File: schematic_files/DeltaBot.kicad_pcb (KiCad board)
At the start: 2 copper layers, 241.5 x 110.5 mm, 15 parts, among them J1 USB C PD Modulle, J2 LIDAR, J3 MOTOR_L, J4 MOTOR_R, SW1 SW_SPDT, U1 RPLIDAR C1, U1 Radxa_ROCK5B, U2 Buck Converter

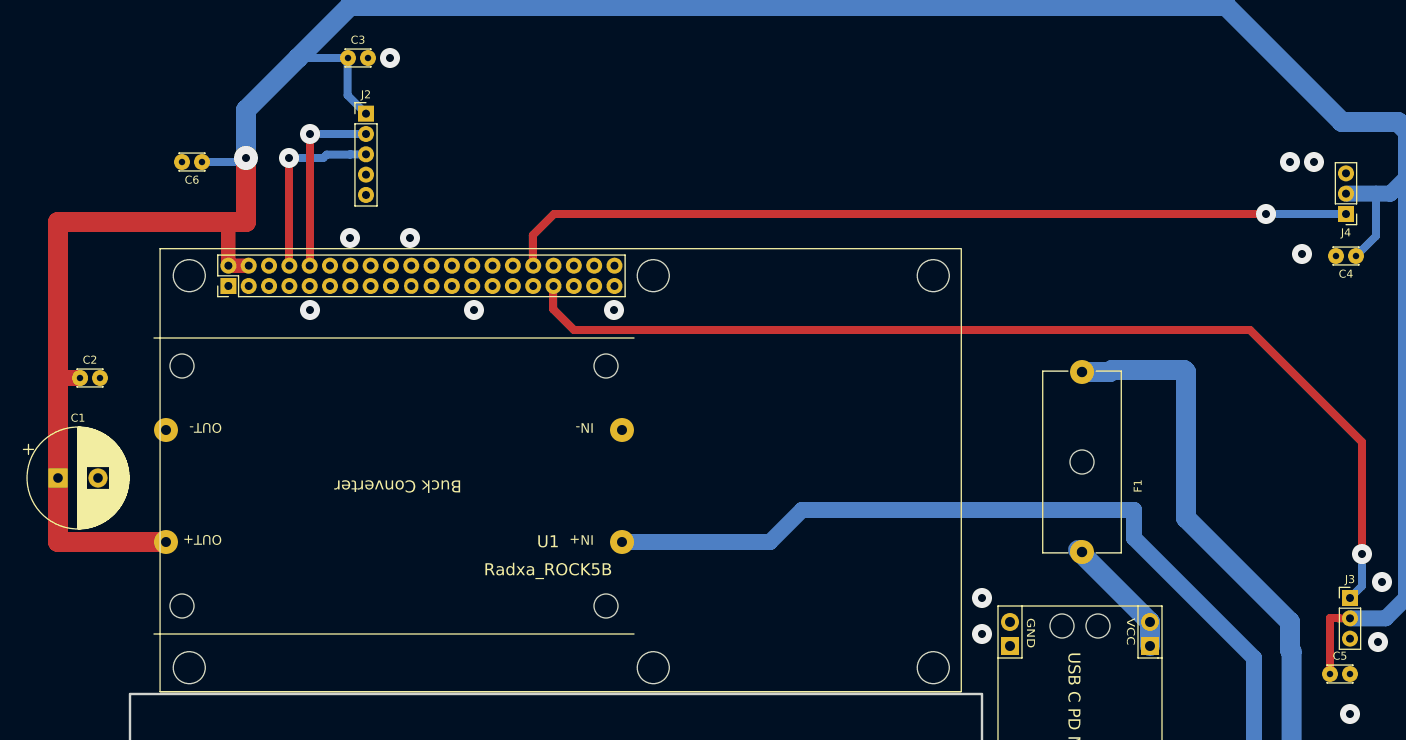
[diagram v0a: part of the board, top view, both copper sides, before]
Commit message: Updated the PCB so that all pads can be soldered without plating through.
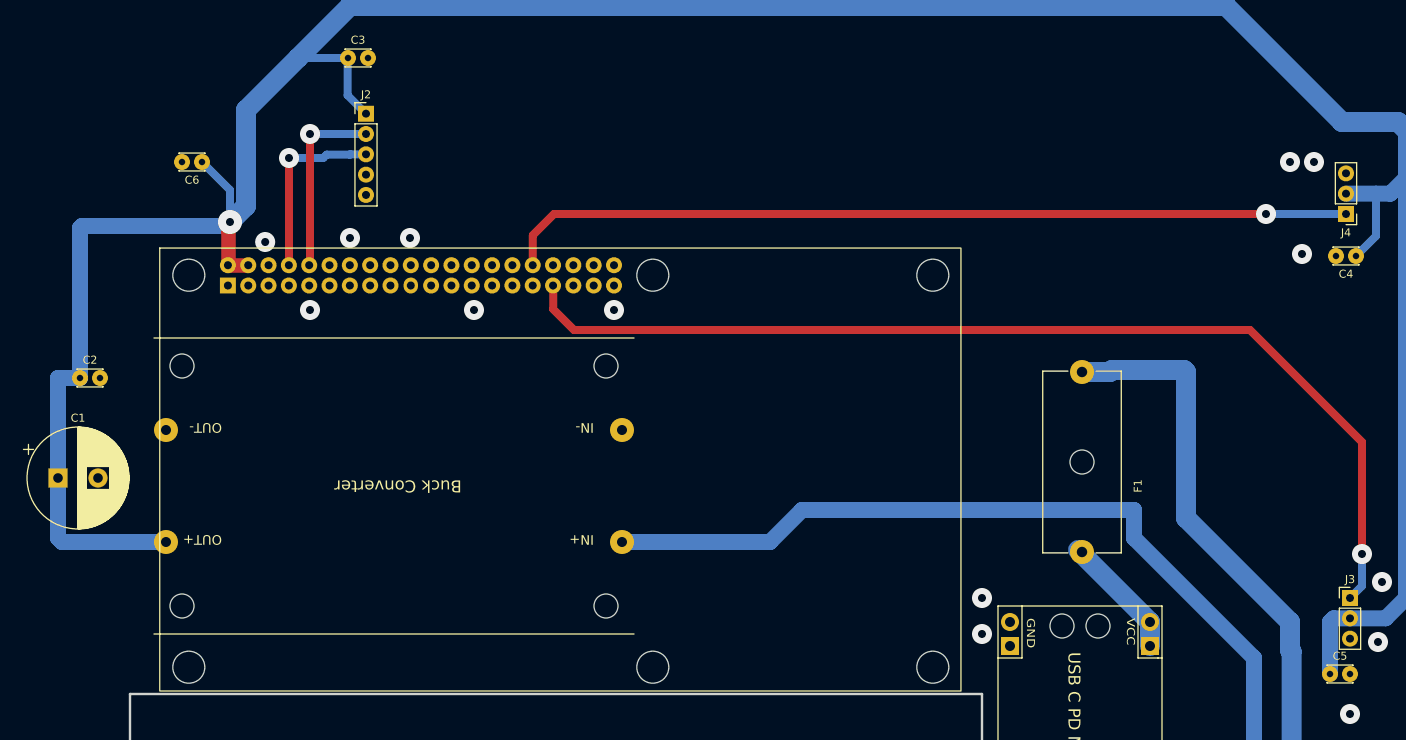
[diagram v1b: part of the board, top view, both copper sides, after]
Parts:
- U1: footprint deltabot:ROCK_5B -> DeltaBotFootprints:ROCK_5B; moved to B.Cu
- moved U1 3.09 mm to (104.8, 108.9), turned to 180 degrees
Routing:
- net +5V: track 372.2 -> 370.4 mm

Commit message: Added an LED to it.
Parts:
- added D1: LED, LED_THT:LED_D5.0mm_Clear, F.Cu at (194.2, 91.0)
- added R1: 330R, Resistor_THT:R_Axial_DIN0207_L6.3mm_D2.5mm_P10.16mm_Horizontal, F.Cu at (202.8, 75.9)
- J2: value LIDAR -> Conn_01x05; footprint deltabot:PinHeader_1x05_P2.54mm_Vertical -> DeltaBotFootprints:PinHeader_1x05_P2.54mm_Vertical
- moved F1 0.25 mm to (168.5, 86.0)
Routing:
- net Net-(D1-A): track 0.00 -> 8.02 mm
- net +5V: track 370.4 -> 374.6 mm
- net PWM_L: track 130.8 -> 129.1 mm

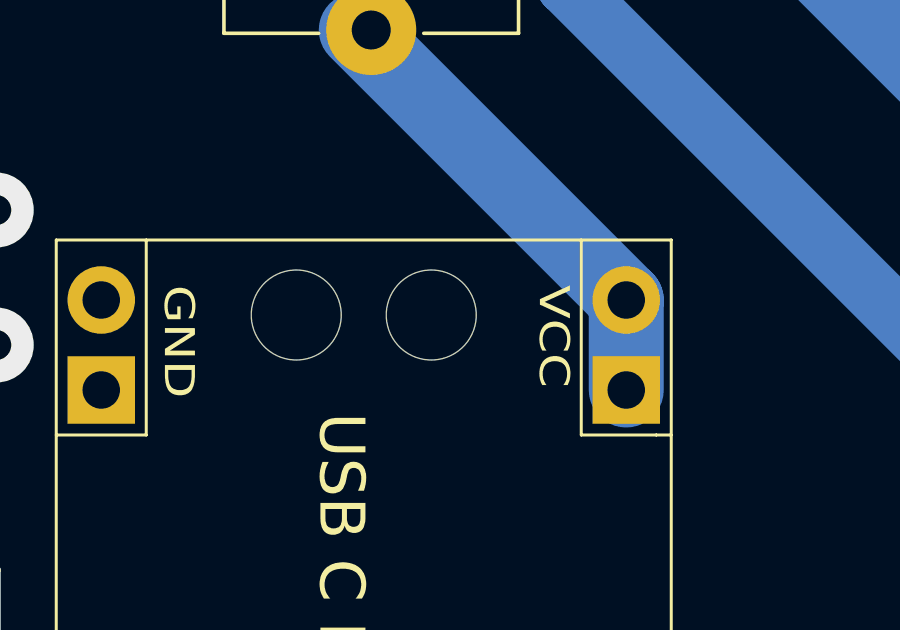
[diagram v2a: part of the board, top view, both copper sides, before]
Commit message: Fixed the USB PD module footprint.
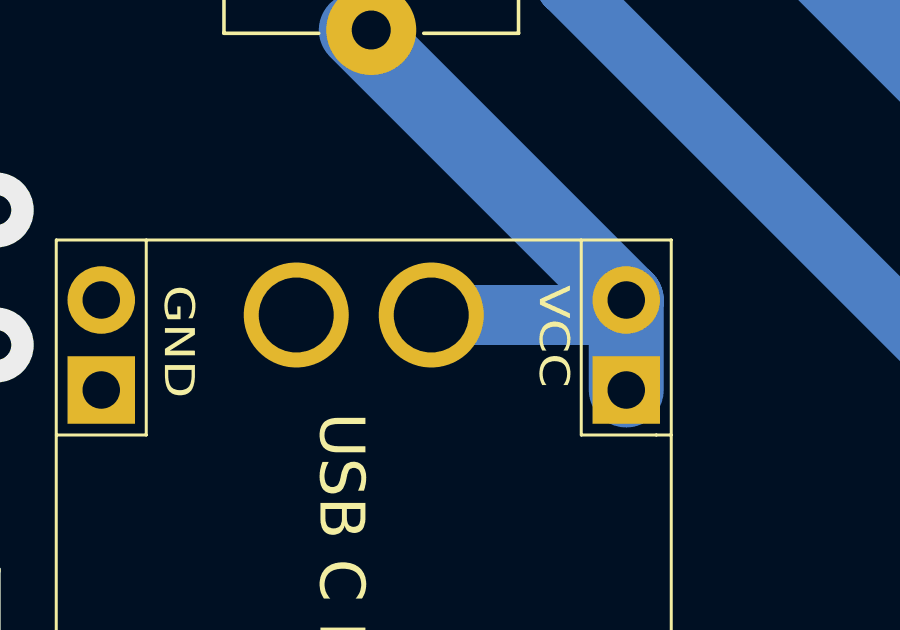
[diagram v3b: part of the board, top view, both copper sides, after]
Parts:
- J1: footprint deltabot:USB_C -> DeltaBotFootprints:USB_C
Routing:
- net Net-(J1-VCC): track 15.7 -> 22.4 mm
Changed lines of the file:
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@@
 		)
 	)
-	(footprint "deltabot:USB_C"
+	(footprint "DeltaBotFootprints:USB_C"
 		(layer "F.Cu")
 		(at 168.5 130.5 -90)
@@
 			(unit
 				(name "A")
-				(pins "1" "2")
+				(pins "3" "4" "1" "2")
 			)
 		)
@@
 			)
 		)
-		(pad "" np_thru_hole circle
-			(at -12.5 -2 270)
-			(size 3 3)
-			(drill 3)
-			(layers "*.Cu" "*.Mask")
-		)
-		(pad "" np_thru_hole circle
-			(at -12.5 2.5 270)
-			(size 2.5 2.5)
-			(drill 3)
-			(layers "*.Cu" "*.Mask")
-		)
 		(pad "1" thru_hole circle
 			(at -13 -8.5 270)
@@
 			(net "Net-(J1-VCC)")
 			(pinfunction "VCC_1")
-			(pintype "passive")
+			(pintype "power_out")
 			(thermal_bridge_angle 90)
 		)
@@
 			(net "Net-(J1-VCC)")
 			(pinfunction "VCC_1")
-			(pintype "passive")
+			(pintype "power_out")
 		)
 		(pad "2" thru_hole circle
@@
 			(net "GND")
 			(pinfunction "GND_2")
-			(pintype "passive")
+			(pintype "power_out")
 			(thermal_bridge_angle 90)
 		)
@@
 			(net "GND")
 			(pinfunction "GND_2")
-			(pintype "passive")
+			(pintype "power_out")
+		)
+		(pad "3" thru_hole circle
+			(at -12.5 -2 270)
+			(size 3.5 3.5)
+			(drill 2.5)
+			(layers "*.Cu" "*.Mask")
+			(remove_unused_layers no)
+			(net "Net-(J1-VCC)")
+			(pinfunction "VCC_3")
+			(pintype "power_out")
+		)
+		(pad "4" thru_hole circle
+			(at -12.5 2.5 270)
+			(size 3.5 3.5)
+			(drill 2.5)
+			(layers "*.Cu" "*.Mask")
+			(remove_unused_layers no)
+			(net "GND")
+			(pinfunction "GND_4")
+			(pintype "power_out")
 		)
 		(embedded_fonts no)
@@
 		(layer "B.Cu")
 		(net "Net-(J1-VCC)")
+	)
+	(segment
+		(start 176.5 118)
+		(end 177 117.5)
+		(width 2)
+		(layer "B.Cu")
+		(net "Net-(J1-VCC)")
+	)
+	(segment
+		(start 170.5 118)
+		(end 176.5 118)
+		(width 2)
+		(layer "B.Cu")
+		(net "Net-(J1-VCC)")

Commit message: Updated the DollaTek Buck converter.
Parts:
- U2: footprint deltabot:BUCK_CONV -> DeltaBotFootprints:BUCK_CONV
- moved U2 7.50 mm to (90.5, 100.5)
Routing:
- net +9V: track 106.4 -> 99.9 mm
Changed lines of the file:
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@@
 		)
 	)
-	(footprint "deltabot:BUCK_CONV"
+	(footprint "DeltaBotFootprints:BUCK_CONV"
 		(layer "F.Cu")
-		(at 83 100.5 180)
+		(at 90.5 100.5 180)
 		(property "Reference" "U2"
 			(at 0 -3.5 180)
@@
 			)
 		)
-		(sheetname "/")
-		(sheetfile "DeltaBot.kicad_sch")
-		(units
-			(unit
-				(name "A")
-				(pins "1" "2" "3" "4")
+		(property "Field4" "${REFERENCE}"
+			(at 0 -7.5 180)
+			(unlocked yes)
+			(layer "F.Fab")
+			(hide yes)
+			(effects
+				(font
+					(size 1 1)
+					(thickness 0.15)
+				)
 			)
 		)
+		(sheetname "/")
+		(sheetfile "DeltaBot.kicad_sch")
 		(attr through_hole)
 		(duplicate_pad_numbers_are_jumpers no)
-		(fp_line
-			(start 30.5 18.5)
-			(end -29.5 18.5)
-			(stroke
-				(width 0.1)
-				(type default)
-			)
-			(layer "F.SilkS")
-		)
-		(fp_line
-			(start -29.5 -18.5)
-			(end 30.5 -18.5)
-			(stroke
-				(width 0.1)
-				(type default)
-			)
-			(layer "F.SilkS")
-		)
-		(fp_line
-			(start 30.5 -18.5)
-			(end 30.5 18.5)
-			(stroke
-				(width 0.1)
-				(type default)
-			)
-			(layer "Dwgs.User")
-		)
-		(fp_line
-			(start -29.5 18.5)
-			(end -29.5 -18.5)
-			(stroke
-				(width 0.1)
-				(type default)
-			)
-			(layer "Dwgs.User")
-		)
 		(fp_rect
 			(start -30.5 -19.5)
-			(end 31.5 19.5)
+			(end 38.5 19.5)
 			(stroke
 				(width 0.1)
@@
 		)
 		(fp_text user "OUT-"
-			(at 22 8 180)
+			(at 26 8 180)
 			(unlocked yes)
 			(layer "F.SilkS")
@@
 		)
 		(fp_text user "OUT+"
-			(at 22 -6 180)
+			(at 26 -6 180)
 			(unlocked yes)
 			(layer "F.SilkS")
@@
 		)
 		(pad "" np_thru_hole circle
-			(at -26 -15 180)
+			(at -26 -16.5 180)
 			(size 3 3)
 			(drill 3)
@@
 		)
 		(pad "" np_thru_hole circle
-			(at -26 15 180)
+			(at -26 16.5 180)
 			(size 3 3)
 			(drill 3)
@@
 		)
 		(pad "" np_thru_hole circle
-			(at 27 -15 180)
+			(at 34 -16.5 180)
 			(size 3 3)
 			(drill 3)
@@
 		)
 		(pad "" np_thru_hole circle
-			(at 27 15 180)
+			(at 34 16.5 180)
 			(size 3 3)
 			(drill 3)
@@
 		)
 		(pad "1" thru_hole circle
-			(at -28 -7 180)
+			(at -27 -7 180)
 			(size 3 3)
 			(drill 1.25)
@@
 		)
 		(pad "2" thru_hole circle
-			(at -28 7 180)
+			(at -27 7 180)
 			(size 3 3)
 			(drill 1.25)
@@
 		)
 		(pad "3" thru_hole circle
-			(at 29 -7 180)
+			(at 35 -7 180)
 			(size 3 3)
 			(drill 1.25)
@@
 		)
 		(pad "4" thru_hole circle
-			(at 29 7 180)
+			(at 35 7 180)
 			(size 3 3)
 			(drill 1.25)
@@
 		)
 		(group ""
-			(members "71852d1f-848b-4fbd-8058-7b7c18c79566" "d77c7138-d943-450b-b308-2ac7d07109fa")
-		)
-		(group ""
-			(members "90b2a300-4ea9-4ddd-beee-bc01a7ce96ee" "c163b686-527c-4015-b9fb-329bd7a7b745"
-				"ce0cf420-a50d-48e5-a98f-5eaaee4e14c5" "fda4a215-f7f3-4819-bc2d-31e87e1292a1"
-			)
-		)
-		(group ""
-			(members "4db89265-00a1-4bf7-9d0e-a5405c16d519" "d65a6a3e-21b7-4699-a39f-50c4af067379"
-				"f7ef2530-fac1-45ac-8080-2da75ab98b6d" "fd23ff6b-d713-4fcd-9328-6d82965ac1e3"
-			)
+			(members "06a10fda-4ba5-4915-be93-18ebe6a4d55a" "a157afaf-f950-4898-b6b6-097cbf784ab5")
 		)
 		(embedded_fonts no)
@@
 	)
 	(segment
-		(start 129.5 107.5)
-		(end 111 107.5)
+		(start 133.5 103.5)
+		(end 129.5 107.5)
 		(width 2)
 		(layer "B.Cu")
@@
 	)
 	(segment
-		(start 175 107)
-		(end 175 103.5)
+		(start 190 122)
+		(end 175 107)
 		(width 2)
 		(layer "B.Cu")
@@
 	)
 	(segment
-		(start 190 138)
-		(end 190 122)
+		(start 175 107)
+		(end 175 103.5)
 		(width 2)
 		(layer "B.Cu")
@@
 	)
 	(segment
-		(start 133.5 103.5)
-		(end 129.5 107.5)
+		(start 190 138)
+		(end 190 122)
 		(width 2)
 		(layer "B.Cu")
@@
 	)
 	(segment
-		(start 190 122)
-		(end 175 107)
+		(start 175 103.5)
+		(end 133.5 103.5)
 		(width 2)
 		(layer "B.Cu")
@@
 	)
 	(segment
-		(start 175 103.5)
-		(end 133.5 103.5)
+		(start 129.5 107.5)
+		(end 117.5 107.5)
 		(width 2)
 		(layer "B.Cu")
